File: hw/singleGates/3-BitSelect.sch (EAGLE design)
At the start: 36 parts, among them Q1 BC817, Q10 BC817, Q11 BC817, Q12 BC817, Q13 BC817, Q14 BC817, Q15 BC817, Q16 BC817, Q17 BC817, Q2 BC817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

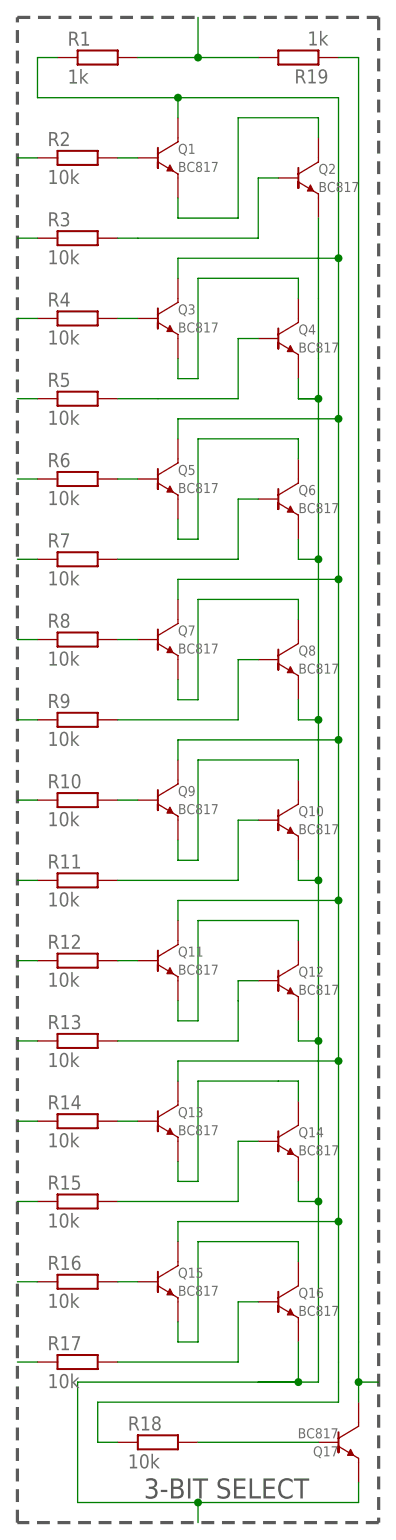
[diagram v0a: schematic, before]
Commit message: fixes some offset and juction issues
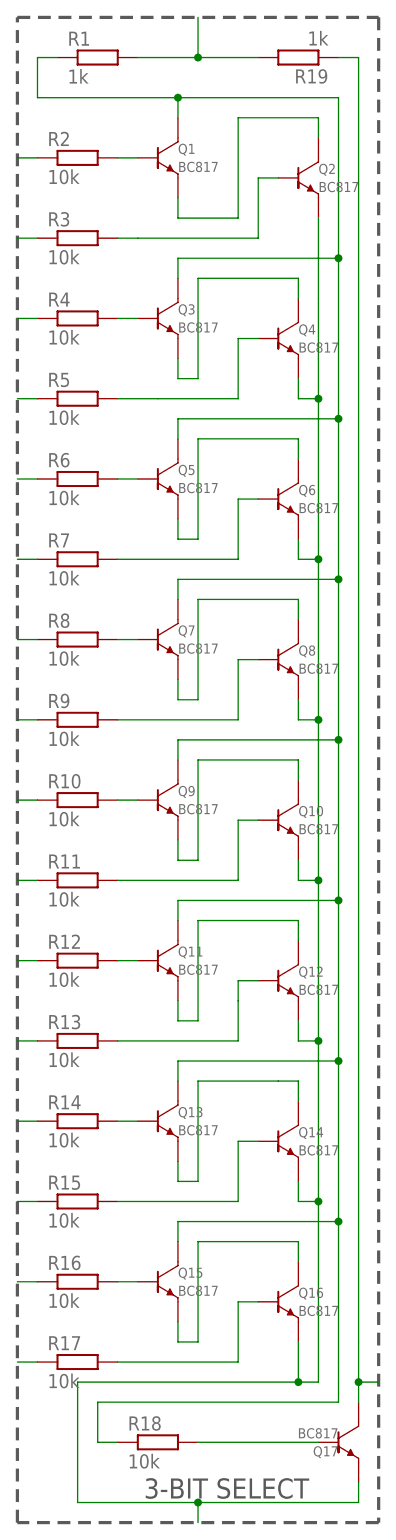
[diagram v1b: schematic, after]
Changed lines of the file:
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@@
 <pinref part="Q2" gate="G$1" pin="EMITTER"/>
 <wire x1="15.24" y1="60.96" x2="15.24" y2="71.12" width="0.1524" layer="91"/>
-<pinref part="Q4" gate="G$1" pin="EMITTER"/>
-<wire x1="12.7" y1="48.26" x2="12.7" y2="50.8" width="0.1524" layer="91"/>
 <wire x1="15.24" y1="60.96" x2="15.24" y2="53.34" width="0.1524" layer="91"/>
 <wire x1="15.24" y1="53.34" x2="15.24" y2="48.26" width="0.1524" layer="91"/>
-<wire x1="15.24" y1="48.26" x2="12.7" y2="48.26" width="0.1524" layer="91"/>
 <pinref part="Q6" gate="G$1" pin="EMITTER"/>
 <wire x1="15.24" y1="27.94" x2="12.7" y2="27.94" width="0.1524" layer="91"/>
 <wire x1="12.7" y1="27.94" x2="12.7" y2="30.48" width="0.1524" layer="91"/>
-<wire x1="12.7" y1="48.26" x2="15.24" y2="48.26" width="0.1524" layer="91"/>
 <wire x1="15.24" y1="48.26" x2="15.24" y2="27.94" width="0.1524" layer="91"/>
 <pinref part="Q8" gate="G$1" pin="EMITTER"/>
@@
 <wire x1="0" y1="-91.44" x2="-15.24" y2="-91.44" width="0.1524" layer="91"/>
 <wire x1="-15.24" y1="-91.44" x2="-15.24" y2="-76.2" width="0.1524" layer="91"/>
-<wire x1="-15.24" y1="-76.2" x2="7.62" y2="-76.2" width="0.1524" layer="91"/>
-<wire x1="7.62" y1="-76.2" x2="12.7" y2="-76.2" width="0.1524" layer="91"/>
+<wire x1="-15.24" y1="-76.2" x2="12.7" y2="-76.2" width="0.1524" layer="91"/>
 <wire x1="12.7" y1="-76.2" x2="12.7" y2="-71.12" width="0.1524" layer="91"/>
 <wire x1="15.24" y1="-53.34" x2="15.24" y2="-76.2" width="0.1524" layer="91"/>
 <wire x1="15.24" y1="-76.2" x2="12.7" y2="-76.2" width="0.1524" layer="91"/>
-<wire x1="12.7" y1="-76.2" x2="7.62" y2="-76.2" width="0.1524" layer="91"/>
 <wire x1="20.32" y1="-88.9" x2="20.32" y2="-91.44" width="0.1524" layer="91"/>
 <pinref part="Q17" gate="G$1" pin="EMITTER"/>
@@
 <junction x="15.24" y="7.62"/>
 <junction x="15.24" y="27.94"/>
-<junction x="15.24" y="48.26"/>
 <junction x="15.24" y="-53.34"/>
 <junction x="0" y="-91.44"/>
 <wire x1="0" y1="-91.44" x2="0" y2="-93.98" width="0.1524" layer="91"/>
 <junction x="12.7" y="-76.2"/>
+<pinref part="Q4" gate="G$1" pin="EMITTER"/>
+<wire x1="12.7" y1="50.8" x2="12.7" y2="48.26" width="0.1524" layer="91"/>
+<wire x1="12.7" y1="48.26" x2="15.24" y2="48.26" width="0.1524" layer="91"/>
+<junction x="15.24" y="48.26"/>
 </segment>
 </net>
